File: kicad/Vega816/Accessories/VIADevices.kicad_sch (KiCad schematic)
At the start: 13 parts, among them J102 VIA Port, U125 RC1602A

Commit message: system controller
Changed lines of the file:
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@@
   (no_connect (at 35.56 125.73))
   (no_connect (at 35.56 128.27))
-  (no_connect (at 38.1 102.87))
-  (no_connect (at 38.1 100.33))
+  (no_connect (at 35.56 102.87))
+  (no_connect (at 35.56 100.33))
   (wire (pts (xy 30.48 115.57) (xy 64.77 115.57))
     (stroke (width 0) (type default) (color 0 0 0 0))
@@
     (stroke (width 0) (type default) (color 0 0 0 0))
   )
-  (wire (pts (xy 30.48 100.33) (xy 38.1 100.33))
+  (wire (pts (xy 30.48 100.33) (xy 35.56 100.33))
     (stroke (width 0) (type default) (color 0 0 0 0))
   )
@@
     (stroke (width 0) (type default) (color 0 0 0 0))
   )
-  (wire (pts (xy 30.48 102.87) (xy 38.1 102.87))
+  (wire (pts (xy 30.48 102.87) (xy 35.56 102.87))
     (stroke (width 0) (type default) (color 0 0 0 0))
   )

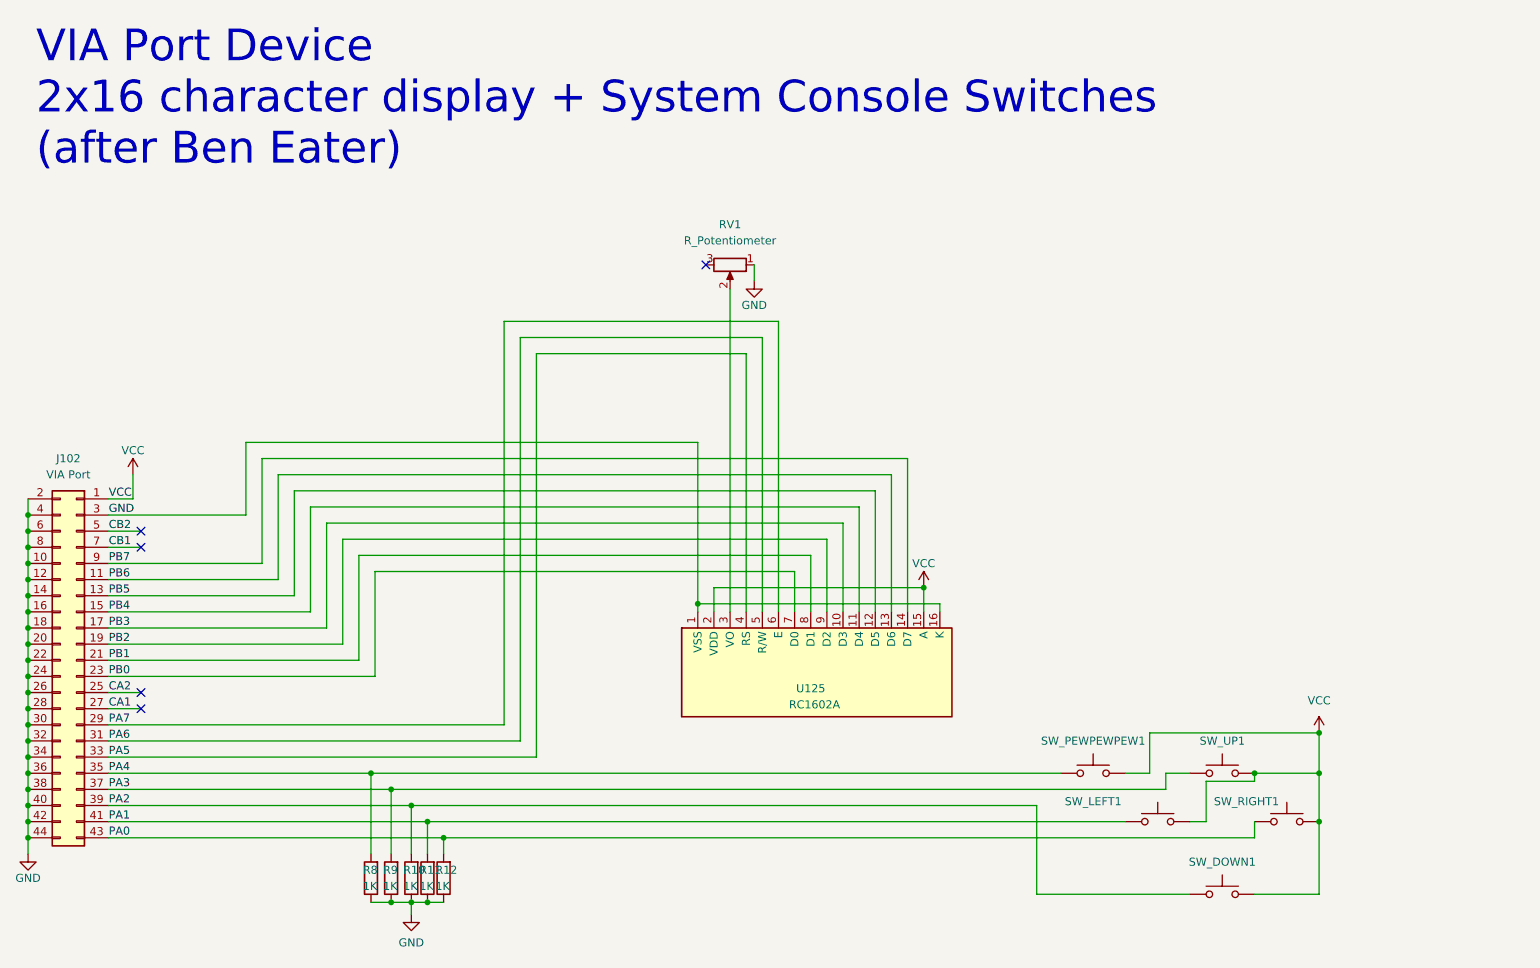
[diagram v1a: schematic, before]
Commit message: via port rework
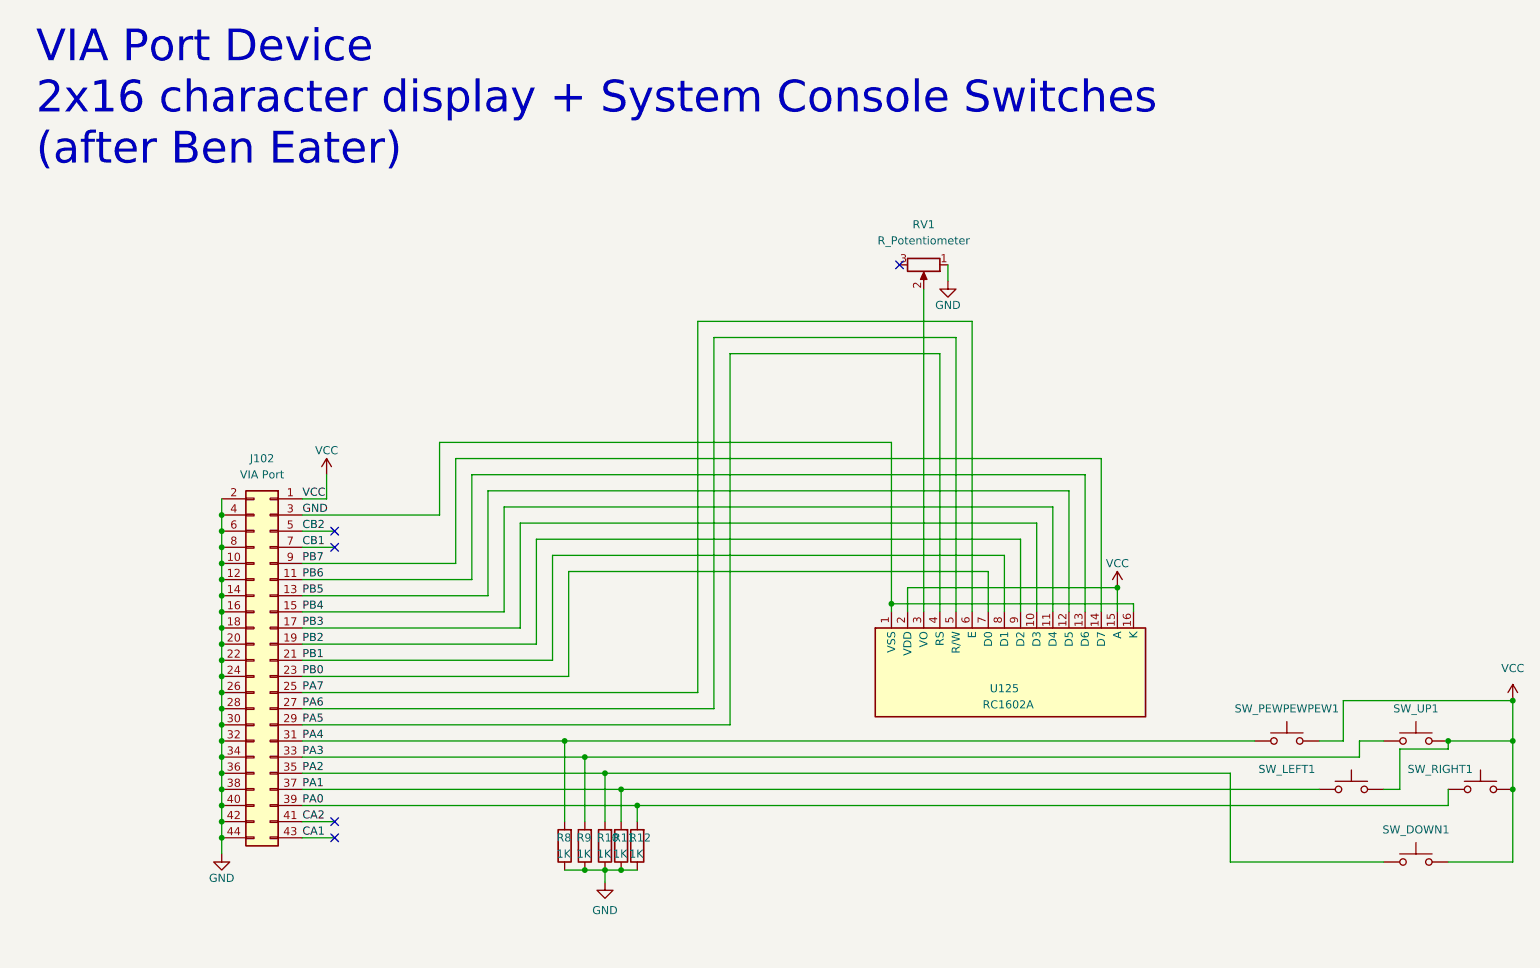
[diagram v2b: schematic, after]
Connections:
- net CA1: now also J102.43 (Pin_43); no longer J102.27 (Pin_27)
- net CA2: now also J102.41 (Pin_41); no longer J102.25 (Pin_25)
- net PA0: now also J102.39 (Pin_39); no longer J102.43 (Pin_43)
- net PA1: now also J102.37 (Pin_37); no longer J102.41 (Pin_41)
- net PA2: now also J102.35 (Pin_35); no longer J102.39 (Pin_39)
- net PA3: now also J102.33 (Pin_33); no longer J102.37 (Pin_37)
- net PA4: now also J102.31 (Pin_31); no longer J102.35 (Pin_35)
- net PA5: now also J102.29 (Pin_29); no longer J102.33 (Pin_33)
- net PA6: now also J102.27 (Pin_27); no longer J102.31 (Pin_31)
- net PA7: now also J102.25 (Pin_25); no longer J102.29 (Pin_29)
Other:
- moved on the sheet: J102, R10, R11, R12, R8, R9, RV1, SW_DOWN1, SW_LEFT1, SW_PEWPEWPEW1, SW_RIGHT1, SW_UP1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

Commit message: via
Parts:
- removed J102: VIA Port, symbol Connector_Generic:Conn_02x22_Odd_Even
- removed R10, R11, R12, R8, R9: 1K, symbol Device:R
- removed SW_DOWN1, SW_LEFT1, SW_PEWPEWPEW1, SW_RIGHT1, SW_UP1: SW_Push, symbol Switch:SW_Push
- removed U125: RC1602A, Display:RC1602A, symbol Vega816:RC1602A
- added J?: VIA Port, symbol Connector_Generic:Conn_02x22_Odd_Even
- added R? (x5): 1K, symbol Device:R
- added SW_DOWN, SW_LEFT, SW_PEWPEW, SW_RIGHT, SW_UP: SW_Push, symbol Switch:SW_Push
- added U?: RC1602A, Display:RC1602A, symbol Vega816:RC1602A
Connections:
- net CA1: now also J?.43 (Pin_43)
- net CA2: now also J?.41 (Pin_41)
- net CB1: now also J?.7 (Pin_7)
- net CB2: now also J?.5 (Pin_5)
- net GND: now also J?.10 (Pin_10), J?.12 (Pin_12), J?.14 (Pin_14), J?.16 (Pin_16), J?.18 (Pin_18), J?.2 (Pin_2), J?.20 (Pin_20), J?.22 (Pin_22), J?.24 (Pin_24), J?.26 (Pin_26), J?.28 (Pin_28), J?.3 (Pin_3), J?.30 (Pin_30), J?.32 (Pin_32), J?.34 (Pin_34), J?.36 (Pin_36), J?.38 (Pin_38), J?.4 (Pin_4), J?.40 (Pin_40), J?.42 (Pin_42), J?.44 (Pin_44), J?.6 (Pin_6), J?.8 (Pin_8), R?.1, R?.1, R?.1, R?.1, R?.1
- net PA0: now also J?.39 (Pin_39), R?.2, SW_UP.1
- net PA1: now also J?.37 (Pin_37), R?.2, SW_DOWN.1
- net PA2: now also J?.35 (Pin_35), R?.2, SW_LEFT.1
- net PA3: now also J?.33 (Pin_33), R?.2, SW_RIGHT.1
- net PA4: now also J?.31 (Pin_31), R?.2, SW_PEWPEW.1
- net PA5: now also J?.29 (Pin_29), U?.4 (RS)
- net PA6: now also J?.27 (Pin_27), U?.5 (R/W)
- net PA7: now also J?.25 (Pin_25), U?.6 (E)
- net PB0: now also J?.23 (Pin_23), U?.7 (D0)
- net PB1: now also J?.21 (Pin_21), U?.8 (D1)
- net PB2: now also J?.19 (Pin_19), U?.9 (D2)
- net PB3: now also J?.17 (Pin_17), U?.10 (D3)
- net PB4: now also J?.15 (Pin_15), U?.11 (D4)
- net PB5: now also J?.13 (Pin_13), U?.12 (D5)
- net PB6: now also J?.11 (Pin_11), U?.13 (D6)
- net PB7: now also J?.9 (Pin_9), U?.14 (D7)
- net VCC: now also J?.1 (Pin_1), SW_DOWN.2, SW_LEFT.2, SW_PEWPEW.2, SW_RIGHT.2, SW_UP.2, U?.15 (A), U?.2 (VDD)
- net at RV1.2: now also U?.3 (VO)
- new net: U?.1 (VSS), U?.16 (K)
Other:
- moved on the sheet: RV1

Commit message: dfsg
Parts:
- removed J?: VIA Port, symbol Connector_Generic:Conn_02x22_Odd_Even
- removed R? (x5): 1K, symbol Device:R
- removed RV1: R_Potentiometer, symbol Device:R_Potentiometer
- removed SW_DOWN, SW_LEFT, SW_PEWPEW, SW_RIGHT, SW_UP: SW_Push, symbol Switch:SW_Push
- removed U?: RC1602A, Display:RC1602A, symbol Vega816:RC1602A
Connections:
- no-connect marks 5 -> 0
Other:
- note removed: "VIA Port Device 2x16 character display + System Console Switches (after Ben Eater)"
